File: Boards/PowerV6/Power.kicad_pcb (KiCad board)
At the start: 4 copper layers, 100 x 100 mm, 205 parts, among them IC1 PIC16F1937, J1 Current Jumper, J2 Current Jumper, J3 Current Jumper, J4 Current Jumper, J5 Current Jumper, J6 Current Jumper, J7 Current Jumper, J8 Current Jumper, K1 Relay(Mech/SSR), K2 Relay(Mech/SSR), K3 Relay(Mech/SSR), K4 Relay(Mech/SSR), K5 Relay(Mech/SSR), K6 Relay(Mech/SSR), K7 Relay(Mech/SSR), K8 Relay(Mech/SSR), P1 L1, P10 L, P11 L, P12 AquaPicBus, P2 L2, P3 L3, P4 L4, P5 L5, P6 L6, P7 L7, P8 L8, P9 ICSP, Q1 2N7002, Q2 2N7002, Q3 2N7002, Q4 2N7002, Q5 2N7002, Q6 2N7002, Q7 2N7002, Q8 2N7002, U10 ACS712, U12 ACS712, U13 TLV272, U15 ACS712, U16 ACS712, U17 TLV272, U18 ACS712, U19 LTV-826, U2 ACS712, U20 LTV-826, U21 ST485EC, U3 TLV272, U5 ACS712, U7 ACS712, U8 TLV272, X1 8MHz

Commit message: working on power refactor
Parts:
- removed C10, C17, C21, C28, C32, C37, C39: 1n, Capacitors_SMD:C_0805
- removed C11, C14, C15, C22, C25, C26, C33, C34, C35, C40, C41, C42, C45: 100nF, Capacitors_SMD:C_0805
- removed C16, C20, C27, C31, C36, C38, C9: 22u, Capacitors_SMD:C_0805
- removed C43: 470pF, Capacitors_SMD:C_0805
- removed C44: 470nF, Capacitors_SMD:C_1812
- removed D20: APT2012, LEDs:LED-0805
- removed D21: SMP4-RGY, A_MyFootPrints:PLCC-4
- removed D22, D23, D24, D25, D26, D27: STPS130A, Diodes_SMD:Diode-SMA_Standard
- removed G***: LOGO, MyFootPrints:AquaPic_Logo_Small
- removed J1, J2, J3, J4, J5, J6, J7, J8: Current Jumper, Pin_Headers:Pin_Header_Straight_1x02
- removed R100, R103, R52, R55, R66, R69, R80, R83, R90, R93: 100K, Resistors_SMD:R_0805
- removed R101, R53, R67, R81, R91: 3K01, Resistors_SMD:R_0805
- removed R102, R107, R45, R50, R51, R54, R59, R64, R65, R68, R73, R78, R79, R82, R87, R88, R89, R92, R97, R98, R99: 10K, Resistors_SMD:R_0805
- removed R104, R42, R56, R70, R84, R94: 1K1, Resistors_SMD:R_0805
- removed R105, R109, R112, R113, R114: 300R, Resistors_SMD:R_0805
- removed R106, R108: 13K, Resistors_SMD:R_2512
- removed R110: 1M, Resistors_SMD:R_2010
- removed R111: 1K, Resistors_SMD:R_2512
- removed R43, R44, R57, R58, R71, R72, R85, R86, R95, R96: 100R, Resistors_SMD:R_0805
- removed REF***: OSHW-Logo2_14.6x12mm_SilkScreen, Symbols:OSHW-Logo2_14.6x12mm_SilkScreen
- removed U10, U12, U15, U16, U18, U5, U7: ACS712, Housings_SOIC:SOIC-8_3.9x4.9mm_Pitch1.27mm
- removed U13, U17, U8: TLV272, Housings_SOIC:SOIC-8_3.9x4.9mm_Pitch1.27mm
- removed U19, U20: LTV-826, A_MyFootPrints:8_SMD_GULL_WING
- removed U21: ST485EC, Housings_SOIC:SOIC-8_3.9x4.9mm_Pitch1.27mm
- added C1: 100nF, Capacitors_SMD:C_0805, F.Cu at (193.7, 55.2)
- added C2: 100nF, Capacitors_SMD:C_0805, F.Cu at (208.5, 40.6)
- added C7: 4u7, Capacitors_SMD:C_0805, F.Cu at (224.9, 25.1)
- added C8: 470nF, Capacitors_SMD:C_1812, F.Cu at (192.4, 37.5)
- added P13: 1x2 5.08, MyFootPrints:Screw_Header_1x2_5.08, F.Cu at (197.9, 7.08)
- added Q10: NX7002AK, TO_SOT_Packages_SMD:SOT-23, F.Cu at (168.5, 42.5)
- added Q11: NX7002AK, TO_SOT_Packages_SMD:SOT-23, F.Cu at (160.5, 42.5)
- added Q12: AO3407A, TO_SOT_Packages_SMD:SOT-23, F.Cu at (238.1, -7.16)
- added Q9: NX7002AK, TO_SOT_Packages_SMD:SOT-23, F.Cu at (215.4, 4.71)
- added R18: 100R, Resistors_SMD:R_0805, F.Cu at (243.9, 1.20)
- added R19: 1K, Resistors_SMD:R_0805, F.Cu at (243.5, -4.25)
- added R20: 10K, Resistors_SMD:R_0805, F.Cu at (188.9, 54.9)
- added R21: 100R, Resistors_SMD:R_0805, F.Cu at (210.9, 35.3)
- added R32: 150R, Resistors_SMD:R_0805, F.Cu at (217.3, 21.1)
- added R33: 150R, Resistors_SMD:R_0805, F.Cu at (191.8, 44.0)
- added R34: 150R, Resistors_SMD:R_0805, F.Cu at (185.0, 53.7)
- added R35: 150R, Resistors_SMD:R_0805, F.Cu at (244.6, -9.71)
- added R4: 1K, Resistors_SMD:R_0805, F.Cu at (240.0, -0.95)
- added R5: 10K, Resistors_SMD:R_0805, F.Cu at (176.6, 60.9)
- added R6: 100R, Resistors_SMD:R_0805, F.Cu at (229.3, 8.91)
- added R7: 1K, Resistors_SMD:R_0805, F.Cu at (224.7, 11.0)
- added U1: ST485EC, Housings_SOIC:SOIC-8_3.9x4.9mm_Pitch1.27mm, F.Cu at (136.1, 54.4)
- added U4: LTV-826, MyFootPrints:8_SMD_GULL_WING, F.Cu at (176.1, 16.0)
- C5: value 22u -> 100nF
- C6: value 1n -> 4u7
- D1, D11, D13, D3, D5, D7, D9: value C503B -> APT2012; footprint LEDs:LED-0805 -> LEDs:LED_0805
- D10, D12, D2, D4, D6, D8: value DB2J310 -> STPS130A; footprint Diodes_SMD:SOD-323 -> Diodes_SMD:D_SMA
- D14: footprint Diodes_SMD:Diode-SMA_Standard -> Diodes_SMD:D_SMA
- D15, D18: value DB2J310 -> APT2012; footprint Diodes_SMD:SOD-323 -> LEDs:LED_0805
- D16: value C503B -> STPS130A; footprint LEDs:LED-0805 -> Diodes_SMD:D_SMA
- D17: value STPS130A -> SMTL4-RGY; footprint Diodes_SMD:Diode-SMA_Standard -> MyFootPrints:PLCC-4
- D19: footprint LEDs:LED-0805 -> LEDs:LED_0805
- IC1: value PIC16F1937 -> PIC32MM0064GPM048; footprint Housings_QFP:TQFP-44_10x10mm_Pitch0.8mm -> Housings_DFN_QFN:QFN-48-1EP_6x6mm_Pitch0.4mm
- K1, K2, K3, K4, K5, K6, K7, K8: footprint A_MyFootPrints:Relay-Mech-SSR -> MyFootPrints:Relay-Mech-SSR
- P1: value L1 -> Stab and 1x3; footprint A_MyFootPrints:Screw_Header_1x1_5.08 -> MyFootPrints:Current_Board
- P10: value L -> 1x6 2.54 Pin Header; footprint MyFootPrints:Screw_Header_1x2_5.08 -> Pin_Headers:Pin_Header_Straight_1x06_Pitch2.54mm
- P11: value L -> Stacked USBA; footprint MyFootPrints:Screw_Header_1x2_5.08 -> MyFootPrints:USB-1.1_Stacked
- P12: value AquaPicBus -> 1x2 5.08; footprint A_MyFootPrints:USB-1.1_Stacked -> MyFootPrints:Screw_Header_1x2_5.08
- P2: value L2 -> Stab and 1x3; footprint A_MyFootPrints:Screw_Header_1x1_5.08 -> MyFootPrints:Current_Board
- P3: value L3 -> Stab and 1x3; footprint A_MyFootPrints:Screw_Header_1x1_5.08 -> MyFootPrints:Current_Board
- P4: value L4 -> Stab and 1x3; footprint A_MyFootPrints:Screw_Header_1x1_5.08 -> MyFootPrints:Current_Board
- P5: value L5 -> Stab and 1x3; footprint A_MyFootPrints:Screw_Header_1x1_5.08 -> MyFootPrints:Current_Board
- P6: value L6 -> Stab and 1x3; footprint A_MyFootPrints:Screw_Header_1x1_5.08 -> MyFootPrints:Current_Board
- P7: value L7 -> Stab and 1x3; footprint A_MyFootPrints:Screw_Header_1x1_5.08 -> MyFootPrints:Current_Board
- P8: value L8 -> Stab and 1x3; footprint A_MyFootPrints:Screw_Header_1x1_5.08 -> MyFootPrints:Current_Board
- P9: value ICSP -> 1x2 2.54; footprint Pin_Headers:Pin_Header_Straight_1x06 -> MyFootPrints:Screw_Header_1x2
- Q1, Q2, Q3, Q4, Q5, Q6, Q7, Q8: value 2N7002 -> NX7002AK; footprint Housings_SOT-23_SOT-143_TSOT-6:SOT-23 -> TO_SOT_Packages_SMD:SOT-23
- R1, R16: value 100R -> 1K
- R10, R13: value 100K -> 1K
- R11, R39: value 3K01 -> 10K
- R12, R3, R9: value 10K -> 100R
- R14: value 1K1 -> 10K
- R2: value 100R -> 10K
- R22: value 10K -> 1K
- R24: value 100K -> 100R
- R25: value 3K01 -> 1K
- R27: value 100K -> 10K
- R28: value 1K1 -> 4K99
- R29, R30: value 100R -> 4K99
- R31: value 10K -> 4K99
- R36: value 10K -> 1M; footprint Resistors_SMD:R_0805 -> Resistors_SMD:R_2010
- R37: value 10K -> 1K; footprint Resistors_SMD:R_0805 -> Resistors_SMD:R_2512
- R38: value 100K -> 300R
- R40: value 10K -> 13K; footprint Resistors_SMD:R_0805 -> Resistors_SMD:R_2512
- R41: value 100K -> 13K; footprint Resistors_SMD:R_0805 -> Resistors_SMD:R_2512
- U2: value ACS712 -> AP2114H; footprint Housings_SOIC:SOIC-8_3.9x4.9mm_Pitch1.27mm -> TO_SOT_Packages_SMD:SOT-223
- U3: value TLV272 -> LTV-826; footprint Housings_SOIC:SOIC-8_3.9x4.9mm_Pitch1.27mm -> MyFootPrints:8_SMD_GULL_WING
- X1: footprint A_MyFootPrints:Resonator_3.2x1.3 -> MyFootPrints:Resonator_3.2x1.3
- moved R27 217.7 mm to (237.5, 9.95), turned to 0 degrees
- moved C4 217.4 mm to (243.6, 6.50)
- moved R26 216.4 mm to (228.2, 19.8), turned to 0 degrees
- moved R24 216.3 mm to (233.6, 9.95), turned to 0 degrees
- moved R17 215.9 mm to (216.5, 26.6), turned to 0 degrees
- moved R16 211.5 mm to (184.4, 59.1), turned to 0 degrees
- moved R15 210.5 mm to (199.6, 44.5), turned to 0 degrees
- moved R25 209.1 mm to (221.2, 21.9), turned to 0 degrees
- moved D4 208.3 mm to (238.6, -14.3), turned to 0 degrees
- moved R14 208.1 mm to (239.4, 4.50), turned to 0 degrees
- moved R23 206.4 mm to (195.7, 49.9), turned to 0 degrees
- moved D3 205.4 mm to (178.3, 55.6), turned to 0 degrees
- moved R28 205.3 mm to (203.9, 44.5), turned to 0 degrees
- moved R22 204.9 mm to (195.7, 44.5), turned to 0 degrees
- moved Q2 199.3 mm to (171.1, 49.5), turned to 0 degrees
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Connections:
- C3 pad 1: +5V -> +3V3
- C4 pad 1: +5V -> Net-(C4-Pad1)
- C5 pad 1: /A_CT1 -> +5V
- C6 pad 1: Net-(C6-Pad1) -> +5V
- D10 pad 2: /A_CT5 -> +5V
- D12 pad 1: Net-(D12-Pad1) -> Net-(D11-Pad1)
- D12 pad 2: /A_CT6 -> +5V
- D14 pad 1: Net-(D1-Pad2) -> Net-(D13-Pad1)
- D15 pad 2: /A_CT7 -> Net-(D15-Pad2)
- D16 pad 1: Net-(D16-Pad1) -> Net-(D15-Pad1)
- D16 pad 2: Net-(D16-Pad2) -> +5V
- D17 pad 2: +5V -> Net-(D17-Pad2)
- D18 pad 1: Net-(D18-Pad1) -> GND
- D18 pad 2: /A_CT8 -> Net-(D18-Pad2)
- D19 pad 2: /AC_PWR_AVAIL -> /AC_AVAIL
- D2 pad 1: Net-(D2-Pad1) -> Net-(D1-Pad1)
- D2 pad 2: /A_CT1 -> +5V
- D3 pad 2: Net-(D17-Pad1) -> Net-(D3-Pad2)
- D4 pad 1: Net-(D4-Pad1) -> Net-(D3-Pad1)
- D4 pad 2: /A_CT2 -> +5V
- D5 pad 2: Net-(D22-Pad1) -> Net-(D5-Pad2)
- D6 pad 1: Net-(D6-Pad1) -> Net-(D5-Pad1)
- D6 pad 2: /A_CT3 -> +5V
- D7 pad 2: Net-(D23-Pad1) -> Net-(D7-Pad2)
- D8 pad 1: Net-(D8-Pad1) -> Net-(D7-Pad1)
- D8 pad 2: /A_CT4 -> +5V
- D9 pad 1: Net-(D9-Pad1) -> Net-(D10-Pad1)
- D9 pad 2: Net-(D24-Pad1) -> Net-(D9-Pad2)
- IC1 pad 1: /RX -> (no net)
- IC1 pad 10: /A_CT8 -> /RELAY_6
- IC1 pad 11: (no net) -> GND
- IC1 pad 12: (no net) -> /RELAY_5
- IC1 pad 13: (no net) -> /RELAY_4
- IC1 pad 14: (no net) -> /RELAY_3
- IC1 pad 15: (no net) -> /RELAY_2
- IC1 pad 16: /PGC -> /RELAY_1
- IC1 pad 17: /PGD -> GND
- IC1 pad 18: //MCLR -> +3V3
- IC1 pad 19: /A_CT1 -> //MCLR
- IC1 pad 2: /RELAY5 -> /AC_AVAIL
- IC1 pad 20: /A_CT2 -> /RX_LV
- IC1 pad 21: /A_CT3 -> /CURRENT_1
- IC1 pad 22: /A_CT4 -> /CURRENT_2
- IC1 pad 23: (no net) -> /CURRENT_3
- IC1 pad 24: Net-(C43-Pad1) -> /CURRENT_4
- IC1 pad 25: /A_CT5 -> /CURRENT_5
- IC1 pad 26: /A_CT6 -> /CURRENT_6
- IC1 pad 27: /A_CT7 -> /CURRENT_7
- IC1 pad 28: +5V -> /CURRENT_8
- IC1 pad 29: GND -> (no net)
- IC1 pad 3: /RELAY6 -> /ZERO_CROSS
- IC1 pad 30: Net-(IC1-Pad30) -> +3V3
- IC1 pad 31: Net-(IC1-Pad31) -> GND
- IC1 pad 32: /STAT_LED_R -> Net-(IC1-Pad32)
- IC1 pad 33: (no net) -> Net-(IC1-Pad33)
- IC1 pad 35: /STAT_LED_G -> (no net)
- IC1 pad 36: /STAT_LED_Y -> (no net)
- IC1 pad 38: /RELAY1 -> //RTS
- IC1 pad 39: /RELAY2 -> /LED_R
- IC1 pad 4: /RELAY7 -> (no net)
- IC1 pad 40: /RELAY3 -> /LED_G
- IC1 pad 41: /RELAY4 -> /LED_Y
- IC1 pad 42: (no net) -> GND
- IC1 pad 43: /T_nR -> +3V3
- IC1 pad 44: /TX -> /TX_LV
- IC1 pad 5: /RELAY8 -> /PGC
- IC1 pad 7: +5V -> Net-(C4-Pad1)
- IC1 pad 8: /AC_PWR_AVAIL -> /RELAY_8
- IC1 pad 9: /ZeroCross -> /RELAY_7
- K1 pad 2-1: /L1-1 -> /L1
- K1 pad 2-2: /L1-1 -> /L1
- K1 pad 4-1: Net-(D1-Pad2) -> Net-(D1-Pad1)
- K1 pad 4-2: Net-(D1-Pad2) -> Net-(D1-Pad1)
- K2 pad 2-1: /L1-2 -> /L2
- K2 pad 2-2: /L1-2 -> /L2
- K2 pad 4-1: Net-(D17-Pad1) -> Net-(D3-Pad1)
- K2 pad 4-2: Net-(D17-Pad1) -> Net-(D3-Pad1)
- K3 pad 2-1: /L1-3 -> /L3
- K3 pad 2-2: /L1-3 -> /L3
- K3 pad 4-1: Net-(D22-Pad1) -> Net-(D5-Pad1)
- K3 pad 4-2: Net-(D22-Pad1) -> Net-(D5-Pad1)
- K4 pad 2-1: /L1-4 -> /L4
- K4 pad 2-2: /L1-4 -> /L4
- K4 pad 4-1: Net-(D23-Pad1) -> Net-(D7-Pad1)
- K4 pad 4-2: Net-(D23-Pad1) -> Net-(D7-Pad1)
- K5 pad 2-1: /L1-5 -> /L5
- K5 pad 2-2: /L1-5 -> /L5
- K5 pad 4-1: Net-(D24-Pad1) -> Net-(D10-Pad1)
- K5 pad 4-2: Net-(D24-Pad1) -> Net-(D10-Pad1)
- K6 pad 2-1: /L1-6 -> /L6
- K6 pad 2-2: /L1-6 -> /L6
- K6 pad 4-1: Net-(D11-Pad2) -> Net-(D11-Pad1)
- K6 pad 4-2: Net-(D11-Pad2) -> Net-(D11-Pad1)
- K7 pad 2-1: /L1-7 -> /L7
- K7 pad 2-2: /L1-7 -> /L7
- K7 pad 4-1: Net-(D13-Pad2) -> Net-(D13-Pad1)
- K7 pad 4-2: Net-(D13-Pad2) -> Net-(D13-Pad1)
- K8 pad 2-1: /L1-8 -> /L8
- K8 pad 2-2: /L1-8 -> /L8
- K8 pad 4-1: Net-(D16-Pad2) -> Net-(D15-Pad1)
- K8 pad 4-2: Net-(D16-Pad2) -> Net-(D15-Pad1)
- P1 pad 1: /L2-1 -> /L1
- P10 pad 1: /L -> //MCLR
- P10 pad 2: /N -> +3V3
- P11 pad 1: /L -> +5V
- P11 pad 2: /N -> /A
- P12 pad 1: +5V -> /L
- P12 pad 2: /D+ -> /N
- P2 pad 1: /L2-2 -> /L2
- P3 pad 1: /L2-3 -> /L3
- P4 pad 1: /L2-4 -> /L4
- P5 pad 1: /L2-5 -> /L5
- P6 pad 1: /L2-6 -> /L6
- P7 pad 1: /L2-7 -> /L7
- P8 pad 1: /L2-8 -> /L8
- P9 pad 1: //MCLR -> Net-(P9-Pad1)
- P9 pad 2: +5V -> GND
- Q1 pad 3: Net-(D1-Pad2) -> Net-(D1-Pad1)
- Q2 pad 3: Net-(D17-Pad1) -> Net-(D3-Pad1)
- Q3 pad 3: Net-(D22-Pad1) -> Net-(D5-Pad1)
- Q4 pad 3: Net-(D23-Pad1) -> Net-(D7-Pad1)
- Q5 pad 3: Net-(D24-Pad1) -> Net-(D10-Pad1)
- Q6 pad 3: Net-(D11-Pad2) -> Net-(D11-Pad1)
- Q7 pad 3: Net-(D13-Pad2) -> Net-(D13-Pad1)
- Q8 pad 3: Net-(D16-Pad2) -> Net-(D15-Pad1)
- R1 pad 1: +5V -> Net-(Q1-Pad1)
- R1 pad 2: Net-(D1-Pad1) -> /RELAY_1
- R10 pad 1: /A_CT1 -> Net-(Q4-Pad1)
- R10 pad 2: GND -> /RELAY_4
- R11 pad 1: Net-(R11-Pad1) -> Net-(Q4-Pad1)
- R11 pad 2: +5V -> GND
- R12 pad 1: Net-(R12-Pad1) -> +5V
- R12 pad 2: Net-(R11-Pad1) -> Net-(D7-Pad2)
- R13 pad 1: Net-(D2-Pad1) -> Net-(Q5-Pad1)
- R13 pad 2: Net-(R12-Pad1) -> /RELAY_5
- R14 pad 1: Net-(R11-Pad1) -> Net-(Q5-Pad1)
- R15 pad 2: Net-(D3-Pad1) -> Net-(D9-Pad2)
- R16 pad 1: Net-(Q2-Pad1) -> Net-(Q6-Pad1)
- R16 pad 2: /RELAY2 -> /RELAY_6
- R17 pad 1: Net-(Q2-Pad1) -> Net-(Q6-Pad1)
- R2 pad 2: /RELAY1 -> GND
- R22 pad 1: Net-(R22-Pad1) -> Net-(Q8-Pad1)
- R22 pad 2: Net-(R22-Pad2) -> /RELAY_8
- R23 pad 1: Net-(R22-Pad1) -> Net-(Q8-Pad1)
- R24 pad 1: /A_CT2 -> +5V
- R24 pad 2: GND -> Net-(D15-Pad2)
- R25 pad 1: Net-(R25-Pad1) -> Net-(Q9-Pad1)
- R25 pad 2: +5V -> //RTS
- R26 pad 1: Net-(R26-Pad1) -> Net-(Q9-Pad1)
- R26 pad 2: Net-(R25-Pad1) -> GND
- R27 pad 1: Net-(D4-Pad1) -> +5V
- R27 pad 2: Net-(R26-Pad1) -> /RTS
- R28 pad 1: Net-(R25-Pad1) -> +3V3
- R28 pad 2: GND -> /TX_LV
- R29 pad 1: +5V -> +3V3
- R29 pad 2: Net-(D5-Pad1) -> /RX_LV
- R3 pad 1: Net-(Q1-Pad1) -> +5V
- R3 pad 2: GND -> Net-(D1-Pad2)
- R30 pad 1: Net-(Q3-Pad1) -> +5V
- R30 pad 2: /RELAY3 -> /TX
- R31 pad 1: Net-(Q3-Pad1) -> +5V
- R31 pad 2: GND -> /RX
- R36 pad 1: Net-(R36-Pad1) -> /N
- R36 pad 2: Net-(R36-Pad2) -> /L
- R37 pad 1: Net-(R36-Pad1) -> /N
- R37 pad 2: GND -> Net-(R37-Pad2)
- R38 pad 1: /A_CT3 -> Net-(D19-Pad1)
- R38 pad 2: GND -> +3V3
- R39 pad 1: Net-(R39-Pad1) -> +3V3
- R39 pad 2: +5V -> /AC_AVAIL
- R40 pad 2: Net-(R39-Pad1) -> /L
- R41 pad 1: Net-(D6-Pad1) -> Net-(R41-Pad1)
- R41 pad 2: Net-(R40-Pad1) -> /N
- R8 pad 1: Net-(R8-Pad1) -> Net-(Q3-Pad1)
- R8 pad 2: Net-(R8-Pad2) -> GND
- R9 pad 1: Net-(R8-Pad1) -> +5V
- R9 pad 2: GND -> Net-(D5-Pad2)
- U2 pad 1: /L1-1 -> GND
- U2 pad 2: /L1-1 -> +3V3
- U2 pad 3: /L2-1 -> +5V
- U2 pad 4: /L2-1 -> (no net)
- U3 pad 1: Net-(D2-Pad1) -> Net-(R37-Pad2)
- U3 pad 2: Net-(R12-Pad1) -> Net-(C8-Pad2)
- U3 pad 3: Net-(R8-Pad1) -> Net-(C8-Pad2)
- U3 pad 4: GND -> Net-(R37-Pad2)
- U3 pad 5: Net-(R22-Pad1) -> GND
- U3 pad 6: Net-(R26-Pad1) -> /AC_AVAIL
- U3 pad 7: Net-(D4-Pad1) -> GND
- U3 pad 8: +5V -> /AC_AVAIL
- X1 pad 1: Net-(IC1-Pad31) -> Net-(IC1-Pad33)
- X1 pad 3: Net-(IC1-Pad30) -> Net-(IC1-Pad32)
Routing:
- net +5V: track 153.2 -> 0.00 mm, vias 36 -> 0
- net GND: track 109.6 -> 0.00 mm, vias 86 -> 0
- net /RELAY2: track 80.0 -> 0.00 mm, vias 4 -> 0
- net /ZeroCross: track 77.8 -> 0.00 mm, vias 3 -> 0
- net /A_CT2: track 68.3 -> 0.00 mm, vias 2 -> 0
- net /A_CT1: track 67.7 -> 0.00 mm, vias 2 -> 0
- net /RELAY4: track 65.4 -> 0.00 mm, vias 6 -> 0
- net /AC_PWR_AVAIL: track 63.7 -> 0.00 mm, vias 2 -> 0
- net /RELAY1: track 60.3 -> 0.00 mm, vias 2 -> 0
- net /A_CT3: track 50.9 -> 0.00 mm, vias 2 -> 0
- net /A_CT4: track 48.6 -> 0.00 mm, vias 2 -> 0
- net /RELAY6: track 42.2 -> 0.00 mm, vias 4 -> 0
- net /RELAY3: track 38.8 -> 0.00 mm, vias 2 -> 0
- net //MCLR: track 35.1 -> 0.00 mm, vias 1 -> 0
- net /A_CT6: track 35.0 -> 0.00 mm, vias 2 -> 0
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- removed copper zone on In2.Cu, net +5V
- removed copper zone on B.Cu, net /L
- removed copper zone on F.Cu, net /L
- removed copper zone on F.Cu, net /L1-1
- removed copper zone on F.Cu, net /L1-2
- removed copper zone on F.Cu, net /L1-3
- removed copper zone on F.Cu, net /L1-4
- removed copper zone on F.Cu, net /L1-5
- removed copper zone on F.Cu, net /L1-6
- removed copper zone on F.Cu, net /L1-7
- removed copper zone on F.Cu, net /L1-8
- removed copper zone on F.Cu, net /L2-1
- removed copper zone on F.Cu, net /L2-2
- removed copper zone on F.Cu, net /L2-3
- removed copper zone on F.Cu, net /L2-4
- removed copper zone on F.Cu, net /L2-5
- removed copper zone on F.Cu, net /L2-6
- removed copper zone on F.Cu, net /L2-7
- removed copper zone on F.Cu, net /L2-8
- removed copper zone on In1.Cu, net GND
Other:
- outline, holes or cut-outs redrawn
- copper layers 4 -> 2
- net class Default: clearance 0.1524 -> 0.2; trace_width 0.254 -> 0.25; via_dia 0.6858 -> 0.6; via_drill 0.3302 -> 0.4
- rule trace_clearance: 0.1524 -> 0.2
- rule trace_min: 0.2032 -> 0.2
- rule via_min_drill: 0.3302 -> 0.3
- rule via_min_size: 0.6858 -> 0.4
- board text removed: "AquaPic Power Rev 1 Skyler Brandt"
- board text removed: "L"
- board text removed: "N"

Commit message: working on power pcb
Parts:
- removed P9: 1x2 2.54, MyFootPrints:Screw_Header_1x2
- removed Q12: AO3407A, TO_SOT_Packages_SMD:SOT-23
- D17, D18, D19: moved to B.Cu
- IC1: footprint Housings_DFN_QFN:QFN-48-1EP_6x6mm_Pitch0.4mm -> Housings_QFP:TQFP-48_7x7mm_Pitch0.5mm
- R38: value 300R -> 150R
- moved R1 216.7 mm to (40.6, -89.5)
- moved R8 208.0 mm to (40.6, -71.1)
- moved R2 205.2 mm to (40.6, -93.3)
- moved R14 205.0 mm to (40.6, -45.7)
- moved R35 204.6 mm to (40.0, -12.7), turned to 270 degrees
- moved R19 204.2 mm to (40.6, -27.3)
- moved D2 203.5 mm to (34.3, -89.5), turned to 180 degrees
- moved R7 200.0 mm to (40.6, -67.3)
- moved R4 199.0 mm to (59.7, -85.1), turned to 180 degrees
- moved C4 197.1 mm to (55.2, -51.4), turned to 225 degrees
- moved Q1 196.5 mm to (40.6, -97.2), turned to 180 degrees
- moved D10 195.6 mm to (34.3, -45.7), turned to 180 degrees
- moved C3 194.2 mm to (45.7, -62.2), turned to 135 degrees
- moved P13 193.8 mm to (4.45, -5.50), turned to 270 degrees
- moved R40 193.1 mm to (14.6, -8.26), turned to 180 degrees
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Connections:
- D19 pad 1: Net-(D19-Pad1) -> /AC_AVAIL
- D19 pad 2: /AC_AVAIL -> Net-(D19-Pad2)
- IC1 pad 1: (no net) -> /RELAY_8
- IC1 pad 10: /RELAY_6 -> (no net)
- IC1 pad 12: /RELAY_5 -> (no net)
- IC1 pad 14: /RELAY_3 -> /RELAY_2
- IC1 pad 15: /RELAY_2 -> (no net)
- IC1 pad 16: /RELAY_1 -> (no net)
- IC1 pad 21: /CURRENT_1 -> /CURRENT_8
- IC1 pad 22: /CURRENT_2 -> /CURRENT_6
- IC1 pad 23: /CURRENT_3 -> /CURRENT_4
- IC1 pad 24: /CURRENT_4 -> /CURRENT_2
- IC1 pad 25: /CURRENT_5 -> /CURRENT_1
- IC1 pad 26: /CURRENT_6 -> /CURRENT_3
- IC1 pad 27: /CURRENT_7 -> /CURRENT_5
- IC1 pad 28: /CURRENT_8 -> /CURRENT_7
- IC1 pad 35: (no net) -> /RELAY_1
- IC1 pad 36: (no net) -> /RELAY_3
- IC1 pad 4: (no net) -> /RELAY_6
- IC1 pad 46: (no net) -> /RELAY_5
- IC1 pad 47: (no net) -> /RELAY_7
- IC1 pad 8: /RELAY_8 -> (no net)
- IC1 pad 9: /RELAY_7 -> (no net)
- R38 pad 1: Net-(D19-Pad1) -> Net-(D19-Pad2)
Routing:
- added copper zone on In2.Cu, net +3V3
- added copper zone on In2.Cu, net +5V
- added copper zone on B.Cu, net /L
- added copper zone on F.Cu, net /L
- added copper zone on B.Cu, net /L1
- added copper zone on F.Cu, net /L1
- added copper zone on B.Cu, net /L2
- added copper zone on F.Cu, net /L2
- added copper zone on B.Cu, net /L3
- added copper zone on F.Cu, net /L3
- added copper zone on B.Cu, net /L4
- added copper zone on F.Cu, net /L4
- added copper zone on B.Cu, net /L5
- added copper zone on F.Cu, net /L5
- added copper zone on B.Cu, net /L6
- added copper zone on F.Cu, net /L6
- added copper zone on B.Cu, net /L7
- added copper zone on F.Cu, net /L7
- added copper zone on B.Cu, net /L8
- added copper zone on F.Cu, net /L8
- added copper zone on In1.Cu, net GND
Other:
- copper layers 2 -> 4
- net class Default: clearance 0.2 -> 0.1524; trace_width 0.25 -> 0.254; via_dia 0.6 -> 0.6858; via_drill 0.4 -> 0.3302
- rule trace_clearance: 0.2 -> 0.1524
- rule trace_min: 0.2 -> 0.2032
- rule via_min_drill: 0.3 -> 0.3302
- rule via_min_size: 0.4 -> 0.6858

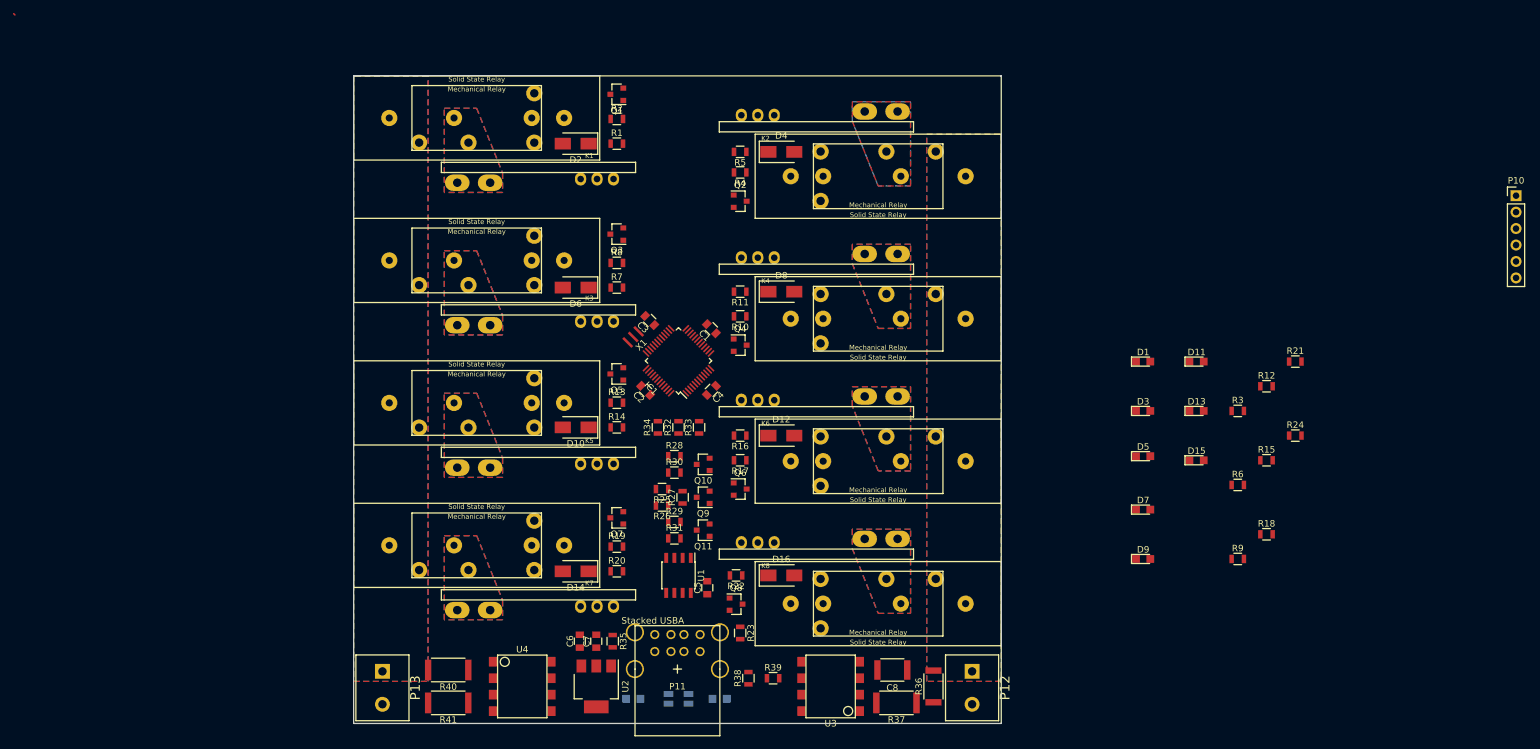
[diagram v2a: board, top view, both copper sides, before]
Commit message: finished power board layout and fixed pin mappings
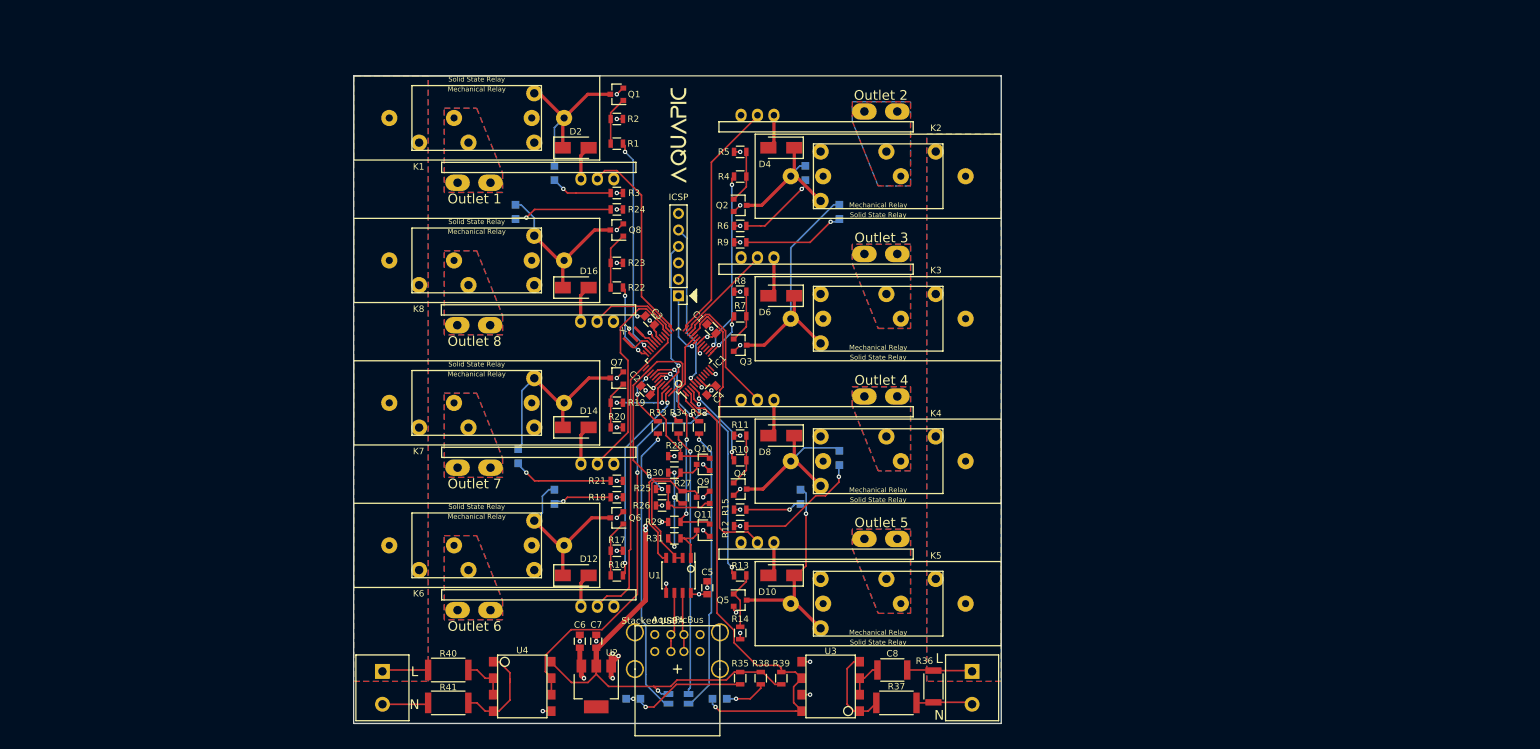
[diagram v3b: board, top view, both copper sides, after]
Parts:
- added G***: LOGO, MyFootPrints:AquaPic_Logo_Small, F.Cu at (50.2, -90.8)
- added REF**: Symbol_OSHW-Logo_SilkScreen, Symbols:Symbol_OSHW-Logo_SilkScreen, B.Cu at (50.0, -20.3)
- D1, D11, D13, D15, D3, D5, D7, D9: moved to B.Cu
- moved ICSP 130.3 mm to (50.2, -66.0), turned to 180 degrees
- moved D15 112.0 mm to (25.0, -79.0), turned to 270 degrees
- moved R24 110.4 mm to (40.6, -79.4), turned to 180 degrees
- moved R21 106.4 mm to (40.6, -37.5), turned to 180 degrees
- moved D13 105.0 mm to (25.4, -41.3), turned to 270 degrees
- moved R3 101.6 mm to (40.6, -81.9), turned to 180 degrees
- moved D11 101.3 mm to (31.0, -35.0), turned to 270 degrees
- moved R18 100.5 mm to (40.6, -34.9), turned to 180 degrees
- moved D1 95.5 mm to (31.0, -85.0), turned to 270 degrees
- moved R9 91.1 mm to (59.7, -74.3)
- moved R6 86.6 mm to (59.7, -76.8)
- moved R12 84.1 mm to (59.7, -30.5)
- moved R15 81.6 mm to (59.7, -33.0)
- moved K8 81.6 mm to (19.0, -71.5), turned to 180 degrees
- moved K5 69.3 mm to (81.0, -18.5), turned to 0 degrees
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- renumbered P10 to ICSP
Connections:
- IC1 pad 1: /RELAY_8 -> /RELAY_5
- IC1 pad 13: /RELAY_4 -> /RELAY_3
- IC1 pad 21: /CURRENT_8 -> /CURRENT_5
- IC1 pad 22: /CURRENT_6 -> /CURRENT_4
- IC1 pad 23: /CURRENT_4 -> /CURRENT_3
- IC1 pad 26: /CURRENT_3 -> /CURRENT_8
- IC1 pad 27: /CURRENT_5 -> /CURRENT_7
- IC1 pad 28: /CURRENT_7 -> /CURRENT_6
- IC1 pad 36: /RELAY_3 -> /RELAY_8
- IC1 pad 39: /LED_R -> /LED_Y
- IC1 pad 4: /RELAY_6 -> /RELAY_4
- IC1 pad 41: /LED_Y -> /LED_R
- IC1 pad 46: /RELAY_5 -> /RELAY_7
- IC1 pad 47: /RELAY_7 -> /RELAY_6
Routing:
- net +3V3: track 0.00 -> 85.5 mm, vias 0 -> 10
- net /AC_AVAIL: track 0.00 -> 76.6 mm, vias 0 -> 1
- net +5V: track 0.00 -> 76.3 mm, vias 0 -> 13
- net /ZERO_CROSS: track 0.00 -> 63.6 mm, vias 0 -> 2
- net GND: track 0.00 -> 50.7 mm, vias 0 -> 39
- net /CURRENT_6: track 0.00 -> 47.9 mm
- net /CURRENT_5: track 0.00 -> 45.1 mm
- net Net-(D17-Pad2): track 0.00 -> 44.8 mm, vias 0 -> 1
- net Net-(D17-Pad1): track 0.00 -> 44.1 mm, vias 0 -> 1
- net Net-(D17-Pad3): track 0.00 -> 41.1 mm, vias 0 -> 1
- net Net-(D5-Pad1): track 0.00 -> 39.7 mm
- net /CURRENT_2: track 0.00 -> 37.8 mm
- net /RX_LV: track 0.00 -> 35.1 mm, vias 0 -> 2
- net Net-(D10-Pad1): track 0.00 -> 34.1 mm, vias 0 -> 1
- net /CURRENT_7: track 0.00 -> 33.7 mm
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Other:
- board text added: "AC Power Available"
- board text added: "AquaPic Power Rev 6.0 Goodtime Development"
- board text added: "AquaPicBus"
- board text added: "L"
- board text added: "N"
- board text added: "Outlet 1"
- board text added: "Outlet 2"
- board text added: "Outlet 3"
- board text added: "Outlet 4"
- board text added: "Outlet 5"
- board text added: "Outlet 6"
- board text added: "Outlet 7"
- board text added: "Outlet 8"
- board text added: "Power Ok"
- board text added: "Status"
